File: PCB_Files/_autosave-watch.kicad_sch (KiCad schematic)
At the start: 118 parts, among them J1 Conn_01x13_MountingPin, J3 Conn_01x02_Pin, P1 USB_C_Plug_USB2.0, Q1 BC847, Q2 BC847, Q3 FS8205A, Q4 BSS138, Q5 BSS138, Q8 BC847, SW1 SW_Push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

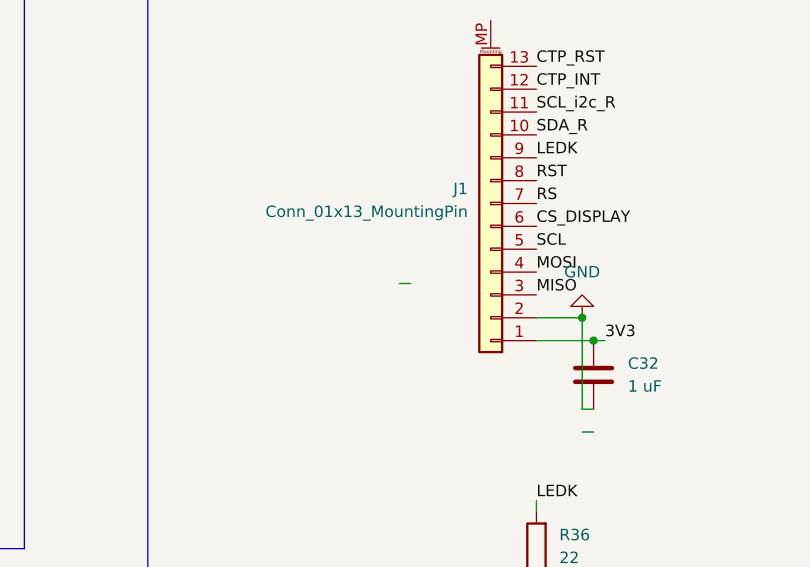
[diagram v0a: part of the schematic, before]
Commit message: Added new ZIF connector footprint and made changes in schematics
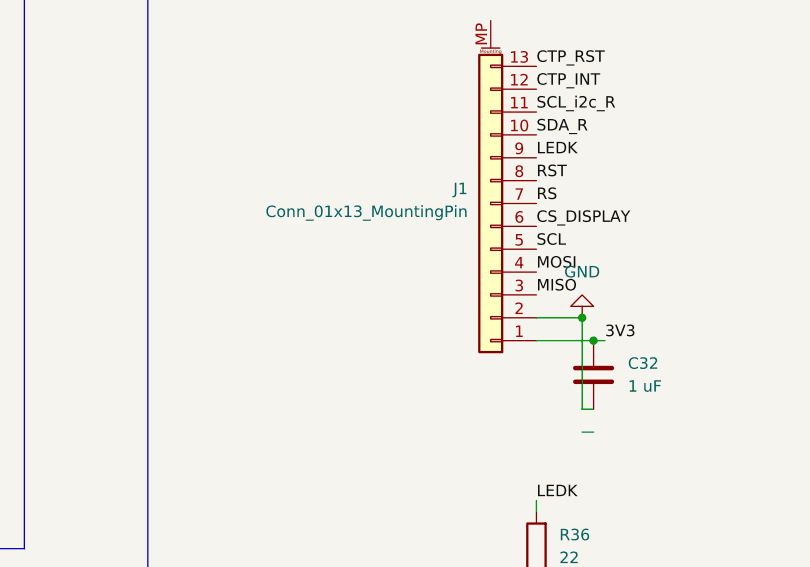
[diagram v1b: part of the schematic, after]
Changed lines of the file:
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@@
-	(wire
-		(pts
-			(xy 408.94 307.34) (xy 410.21 307.34)
-		)
-		(stroke
-			(width 0)
-			(type default)
-		)
-	)
 	(wire
 		(pts
